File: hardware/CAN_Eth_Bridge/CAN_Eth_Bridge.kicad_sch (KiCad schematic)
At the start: 25 parts, among them J102 Global LV and CAN, J105 Conn_02x05_Odd_Even, J106 uart, SW101 SW_Push, U101 MCP2542FDxMF, U103 XMSM0G3507SDGS28R

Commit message: long 88 can stick
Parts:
- removed F101: ~1A, Fuse:Fuseholder_Blade_Mini_Keystone_3568, symbol Device:Fuse_Small
- removed J105: Conn_02x05_Odd_Even, Connector_PinHeader_1.27mm:PinHeader_2x05_P1.27mm_Vertical_SMD, symbol Connector_Generic:Conn_02x05_Odd_Even
- removed J106: uart, Connector_PinHeader_2.54mm:PinHeader_1x03_P2.54mm_Vertical, symbol Connector:Conn_01x03_Pin
- added C101, C102, C103: 220n, Capacitor_SMD:C_0805_2012Metric_Pad1.18x1.45mm_HandSolder, symbol Device:C_Small
- added D101: TS4148, Diode_SMD:D_0805_2012Metric_Pad1.15x1.40mm_HandSolder, symbol Device:D_Small
- added FL102: Choke_CommonMode_FerriteCore_1243, Inductor_SMD:L_CommonModeChoke_Coilcraft_1812CAN, symbol Filter:Choke_CommonMode_FerriteCore_1243
- added J101: Conn_01x05_Pin, Connector_PinHeader_2.54mm:PinHeader_1x05_P2.54mm_Vertical, symbol Connector:Conn_01x05_Pin
- added SW102: SW_DIP_x06, Button_Switch_SMD:SW_DIP_SPSTx06_Slide_Copal_CHS-06B_W7.62mm_P1.27mm, symbol Switch:SW_DIP_x06
- added U102: AP7384-50SA, Package_TO_SOT_SMD:SOT-23-3, symbol Regulator_Linear:AP7384-50SA
- added U104: AP7381-33SA-7, Package_TO_SOT_SMD:SOT-23, symbol Regulator_Linear:AP7381-33SA-7
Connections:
- net GLV- is gone; now on net GND: J102.2 (Pin_2)
- net +3.3V: now also U103.7 (VDD), C101.1, U104.2 (VO)
- net +5V: now also C102.1, U102.2 (VO)
- net GLV+: now also D101.2 (A)
- net GND: now also U103.8 (VSS), C101.2, C102.2, C103.2, J101.1 (Pin_1), U102.3 (GND), U104.3 (GND)
- net G_CAN+: now also FL102.1; no longer U101.7 (CANH)
- net G_CAN-: now also FL102.4; no longer U101.6 (CANL)
- net XDS_RXD: now also J101.3 (Pin_3)
- net XDS_TCK_SWDCLK: now also U103.23 (PA20/SWCLK), J101.5 (Pin_5)
- net XDS_TMS_SWDIO: now also U103.22 (PA19/SWDIO), J101.4 (Pin_4)
- net XDS_TXD: now also J101.2 (Pin_2)
- net vcore: now also U103.3 (VCORE)
- net at R112.1, SW101.1: now also U103.6 (NRST)
- net at U103.9 (PA2_/_ROSC): now also R111.2
- new net: C103.1, D101.1 (K), U102.1 (VI), U104.1 (VI)
- new net: FL102.3, U101.6 (CANL)
- new net: FL102.2, U101.7 (CANH)
- no-connect marks 4 -> 0
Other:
- removed sheet GLV PSU
- note added: "PSU"
- note removed: "- LV only. no HV present - (10,35]VDC GLV working - swap relays for >12VDC operation - IL assumed to share GLV GND - IL sense diode set for ~12VDC"
- note removed: "PWR"
- note removed: "SWD fish"
- moved on the sheet: C104, D103, D104, D105, D106, J102, R107, R108, R109, R110, U101, U103

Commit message: shuffled
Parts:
- renumbered C103 to C101, C104 to C102, C102 to C103, C101 to C104, C107 to C105, C108 to C106, C109 to C107, C110 to C108, D103 to D102, D105 to D103, D106 to D105, FL102 to FL101, J102 to J101, J101 to J102, R108 to R101, R110 to R102, R107 to R103, R109 to R104, R111 to R105, R112 to R106, SW102 to SW101, SW101 to SW102, U102 to U101, U104 to U102, U101 to U103, U103 to U104
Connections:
- net can.rx: now also U104.2 (PA27/RTC_OUT/A0_0)
- net can.tx: now also U104.1 (PA26/A0_1)
- net eth.MISO/POCI: now also U104.19 (PA16/A1_1/FCC_IN)
- net eth.MOSI/PICO: now also U104.21 (PA18/A1_3)
- net eth.SCLK: now also U104.20 (PA17/A1_2)

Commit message: hdd failure D:
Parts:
- removed C102: 220n, Capacitor_SMD:C_0805_2012Metric_Pad1.18x1.45mm_HandSolder, symbol Device:C_Small
- removed D103: red, LED_SMD:LED_0805_2012Metric_Pad1.15x1.40mm_HandSolder, symbol Device:LED_Small
- removed D104: yellow, LED_SMD:LED_0805_2012Metric_Pad1.15x1.40mm_HandSolder, symbol Device:LED_Small
- removed H101, H102, H103: MountingHole, MountingHole:MountingHole_3.2mm_M3, symbol Mechanical:MountingHole
- removed R101: 2.4k, Resistor_SMD:R_0805_2012Metric_Pad1.20x1.40mm_HandSolder, symbol Device:R_Small_US
- removed R106: 40.2k, Resistor_SMD:R_0805_2012Metric_Pad1.20x1.40mm_HandSolder, symbol Device:R_Small_US
- removed SW101: SW_DIP_x06, Button_Switch_SMD:SW_DIP_SPSTx06_Slide_Copal_CHS-06B_W7.62mm_P1.27mm, symbol Switch:SW_DIP_x06
- C107, C108: now not fitted; now left out of the parts list
- D102: value yellow -> green; mouser https://www.mouser.com/ProductDetail/Inolux/IN-S85CS5Y?qs=s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 -> https://www.mouser.com/ProductDetail/Inolux/IN-S85CS5G?qs=s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; specs 5mA, 75mW, 1.8Vf, 5Vr, 589nm, 35mcd -> 5mA, 90mW, 2.5Vf, 5Vr, 525nm, 230mcd; unit x1 0.22 -> 0.27; unit x10 0.15 -> 0.187
- R102: value 3.32k -> 2.4k; mouser https://www.mouser.com/ProductDetail/Walsin/WR08X3321FTL?qs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 -> https://www.mouser.com/ProductDetail/Panasonic/ERJ-P06J242V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; specs 3.32kOhm, 1%, 150V, 125mW, 100ppm, -55C, 155C -> (none); specs  (none) -> 500mW, 5%, 200ppm, 400V, -55C, +155C, anti-surge, TF; unit x1 0.10 -> 0.12; unit x10 0.019 -> 0.039
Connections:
- net led.BMSFault is gone; now on net +3.3V: R104.2
- net led.i2 is gone; now on net GND: R103.2
- net +3.3V: now also U104.24 (PA21/A1_7/VREF-)
- net GND: now also R102.2; no longer D102.1 (K), R102.1
- net XDS_RXD: now also J102.2 (Pin_2), U104.15 (PA10/CLK_OUT); no longer J102.3 (Pin_3)
- net XDS_TXD: now also J102.3 (Pin_3), U104.16 (PA11); no longer J102.2 (Pin_2)
- net eth.cs_N: now also U104.13 (PA6/HFCLK_IN/HFXOUT)
- net eth.irq_N: now also U104.12 (PA5/HFXIN/FCC_IN)
- net eth.reset_N: now also U104.14 (PA9_/_RTC_OUT_/_CLK_OUT)
- net led.i1: now also D102.2 (A), U104.28 (PA25/A0_2)
- net led.sched: now also U104.27 (PA24/A0_3)
- net at R103.1: now also D105.1 (K); no longer D102.2 (A)
- net at SW102.1, U104.6 (NRST): now also R104.1
- new net: D102.1 (K), R102.1
- no-connect marks 0 -> 8
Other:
- note removed: "BMS Fault"
- note removed: "indicator 2"
- moved on the sheet: D105, R103

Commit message: civilized note taking
and untaking !?!?!
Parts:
- added R101: 10, Resistor_SMD:R_0805_2012Metric_Pad1.20x1.40mm_HandSolder, symbol Device:R_Small_US
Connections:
- net GLV+: now also R101.2; no longer D101.2 (A)
- new net: D101.2 (A), R101.1
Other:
- note added: "dinky surge supression"
- moved on the sheet: C101, C103, C104, D101, U101, U102

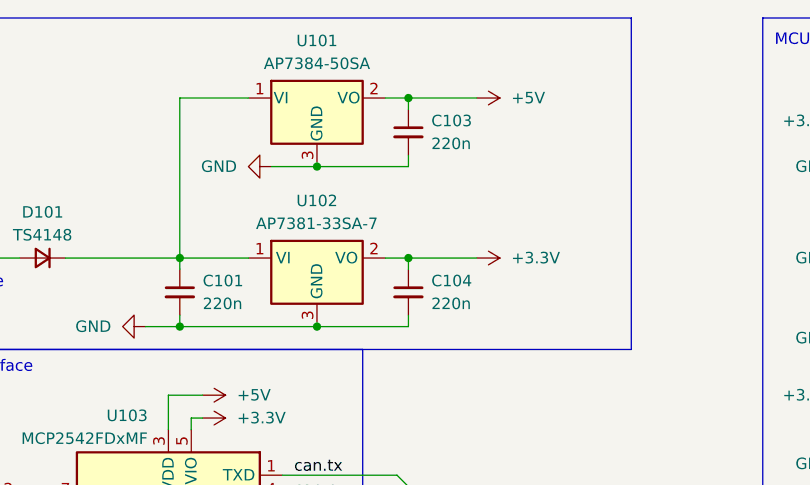
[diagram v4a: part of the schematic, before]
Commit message: pain :(
the 3v3 rail is a 1v rail. double deckering the LDO's didnt fix it :((( . needs new board
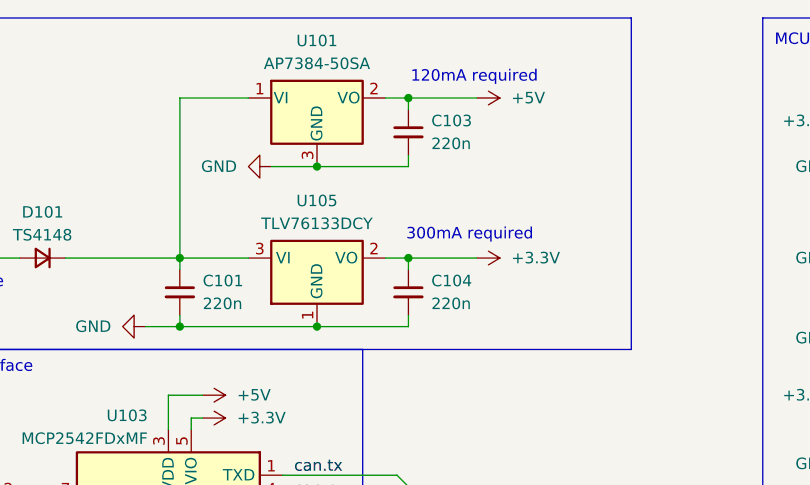
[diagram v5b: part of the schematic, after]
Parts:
- removed U102: AP7381-33SA-7, Package_TO_SOT_SMD:SOT-23, symbol Regulator_Linear:AP7381-33SA-7
- added U105: TLV76133DCY, Package_TO_SOT_SMD:SOT-223-3_TabPin2, symbol Regulator_Linear:TLV76133DCY
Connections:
- net +3.3V: now also U105.2 (VO)
- net GND: now also U105.1 (GND)
- net at C101.1, D101.1 (K), U101.1 (VI): now also U105.3 (VI)
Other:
- note added: "120mA required"
- note added: "300mA required"
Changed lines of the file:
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@@
 		)
 	)
+	(text "120mA required"
+		(exclude_from_sim no)
+		(at 114.554 20.066 0)
+		(effects
+			(font
+				(size 1.27 1.27)
+				(color 194 0 194 1)
+			)
+			(justify left bottom)
+		)
+	)
 	(text "indicator 1"
 		(exclude_from_sim no)
@@
 		)
 	)
+	(text "300mA required"
+		(exclude_from_sim no)
+		(at 114.046 37.592 0)
+		(effects
+			(font
+				(size 1.27 1.27)
+				(color 194 0 194 1)
+			)
+			(justify left bottom)
+		)
+	)
 	(text "dinky surge\nsupression"
 		(exclude_from_sim no)
@@
 	)
 	(junction
-		(at 104.14 46.99)
-		(diameter 0)
-		(color 0 0 0 0)
-	)
-	(junction
 		(at 88.9 46.99)
 		(diameter 0)
@@
 	)
 	(junction
+		(at 104.14 46.99)
+		(diameter 0)
+		(color 0 0 0 0)
+	)
+	(junction
 		(at 259.08 35.56)
 		(diameter 0)
@@
 	(wire
 		(pts
-			(xy 104.14 46.99) (xy 114.3 46.99)
+			(xy 88.9 46.99) (xy 104.14 46.99)
 		)
 		(stroke
@@
 	(wire
 		(pts
-			(xy 88.9 46.99) (xy 104.14 46.99)
-		)
-		(stroke
-			(width 0)
-			(type default)
-		)
-	)
-	(wire
-		(pts
 			(xy 114.3 21.59) (xy 111.76 21.59)
 		)
@@
 	(wire
 		(pts
+			(xy 104.14 46.99) (xy 114.3 46.99)
+		)
+		(stroke
+			(width 0)
+			(type default)
+		)
+	)
+	(wire
+		(pts
 			(xy 111.76 39.37) (xy 114.3 39.37)
 		)
@@
 	)
 	(symbol
+		(lib_id "Regulator_Linear:TLV76133DCY")
+		(at 104.14 39.37 0)
+		(unit 1)
+		(exclude_from_sim no)
+		(in_bom yes)
+		(on_board yes)
+		(dnp no)
+		(fields_autoplaced yes)
+		(property "Reference" "U105"
+			(at 104.14 33.02 0)
+			(effects
+				(font
+					(size 1.27 1.27)
+				)
+			)
+		)
+		(property "Value" "TLV76133DCY"
+			(at 104.14 35.56 0)
+			(effects
+				(font
+					(size 1.27 1.27)
+				)
+			)
+		)
+		(property "Footprint" "Package_TO_SOT_SMD:SOT-223-3_TabPin2"
+			(at 104.14 50.8 0)
+			(effects
+				(font
+					(size 1.27 1.27)
+				)
+				(hide yes)
+			)
+		)
+		(property "Datasheet" "https://www.ti.com/lit/ds/symlink/tlv761.pdf"
+			(at 104.14 53.34 0)
+			(effects
+				(font
+					(size 1.27 1.27)
+				)
+				(hide yes)
+			)
+		)
+		(property "Description" "3.3V, 1A, Low Noise, High-PSRR LDO Regulator, 2.5V...16V input, SOT-223"
+			(at 104.14 39.37 0)
+			(effects
+				(font
+					(size 1.27 1.27)
+				)
+				(hide yes)
+			)
+		)
+		(pin "2"
+		)
+		(pin "3"
+		)
+		(pin "1"
+		)
+		(instances
+			(project ""
+				(path "/20ac6af0-79b5-4ba6-aad3-75081d02c913"
+					(reference "U105")
+					(unit 1)
+				)
+			)
+		)
+	)
+	(symbol
 		(lib_id "zzLocalLibrary:XMSM0G3507SDGS28R")
 		(at 242.57 113.03 0)
@@
 					(unit 1)
 				)
-			)
-		)
-	)
-	(symbol
-		(lib_id "Regulator_Linear:AP7381-33SA-7")
-		(at 104.14 39.37 0)
-		(unit 1)
-		(exclude_from_sim no)
-		(in_bom yes)
-		(on_board yes)
-		(dnp no)
-		(fields_autoplaced yes)
-		(property "Reference" "U102"
-			(at 104.14 33.02 0)
-			(effects
-				(font
-					(size 1.27 1.27)
-				)
-			)
-		)
-		(property "Value" "AP7381-33SA-7"
-			(at 104.14 35.56 0)
-			(effects
-				(font
-					(size 1.27 1.27)
-				)
-			)
-		)
-		(property "Footprint" "Package_TO_SOT_SMD:SOT-23"
-			(at 104.14 49.53 0)
-			(effects
-				(font
-					(size 1.27 1.27)
-				)
-				(hide yes)
-			)
-		)
-		(property "Datasheet" "https://www.diodes.com/assets/Datasheets/AP7381.pdf"
-			(at 104.14 52.07 0)
-			(effects
-				(font
-					(size 1.27 1.27)
-				)
-				(hide yes)
-			)
-		)
-		(property "Description" "150mA Low Dropout Voltage Regulator, Fixed Output 3.3V, Wide Input Voltage Range 40V, SOT-23"
-			(at 104.14 54.61 0)
-			(effects
-				(font
-					(size 1.27 1.27)
-				)
-				(hide yes)
-			)
-		)
-		(property "mouser" "https://www.mouser.com/ProductDetail/Diodes-Incorporated/AP7381-33SA-7?qs=y6ZabgHbY%252ByfboEZm%252BnPlA%3D%3D"
-			(at 104.14 39.37 0)
-			(effects
-				(font
-					(size 1.27 1.27)
-				)
-				(hide yes)
-			)
-		)
-		(property "unit x10" "0.134"
-			(at 104.14 39.37 0)
-			(effects
-				(font
-					(size 1.27 1.27)
-				)
-				(hide yes)
-			)
-		)
-		(property "unit x1" "0.19"
-			(at 104.14 39.37 0)
-			(effects
-				(font
-					(size 1.27 1.27)
-				)
-				(hide yes)
-			)
-		)
-		(pin "1"
-		)
-		(pin "3"
-		)
-		(pin "2"
-		)
-		(instances
-			(project "CAN_Eth_Bridge"
-				(path "/20ac6af0-79b5-4ba6-aad3-75081d02c913"
-					(reference "U102")
-					(unit 1)
-				)

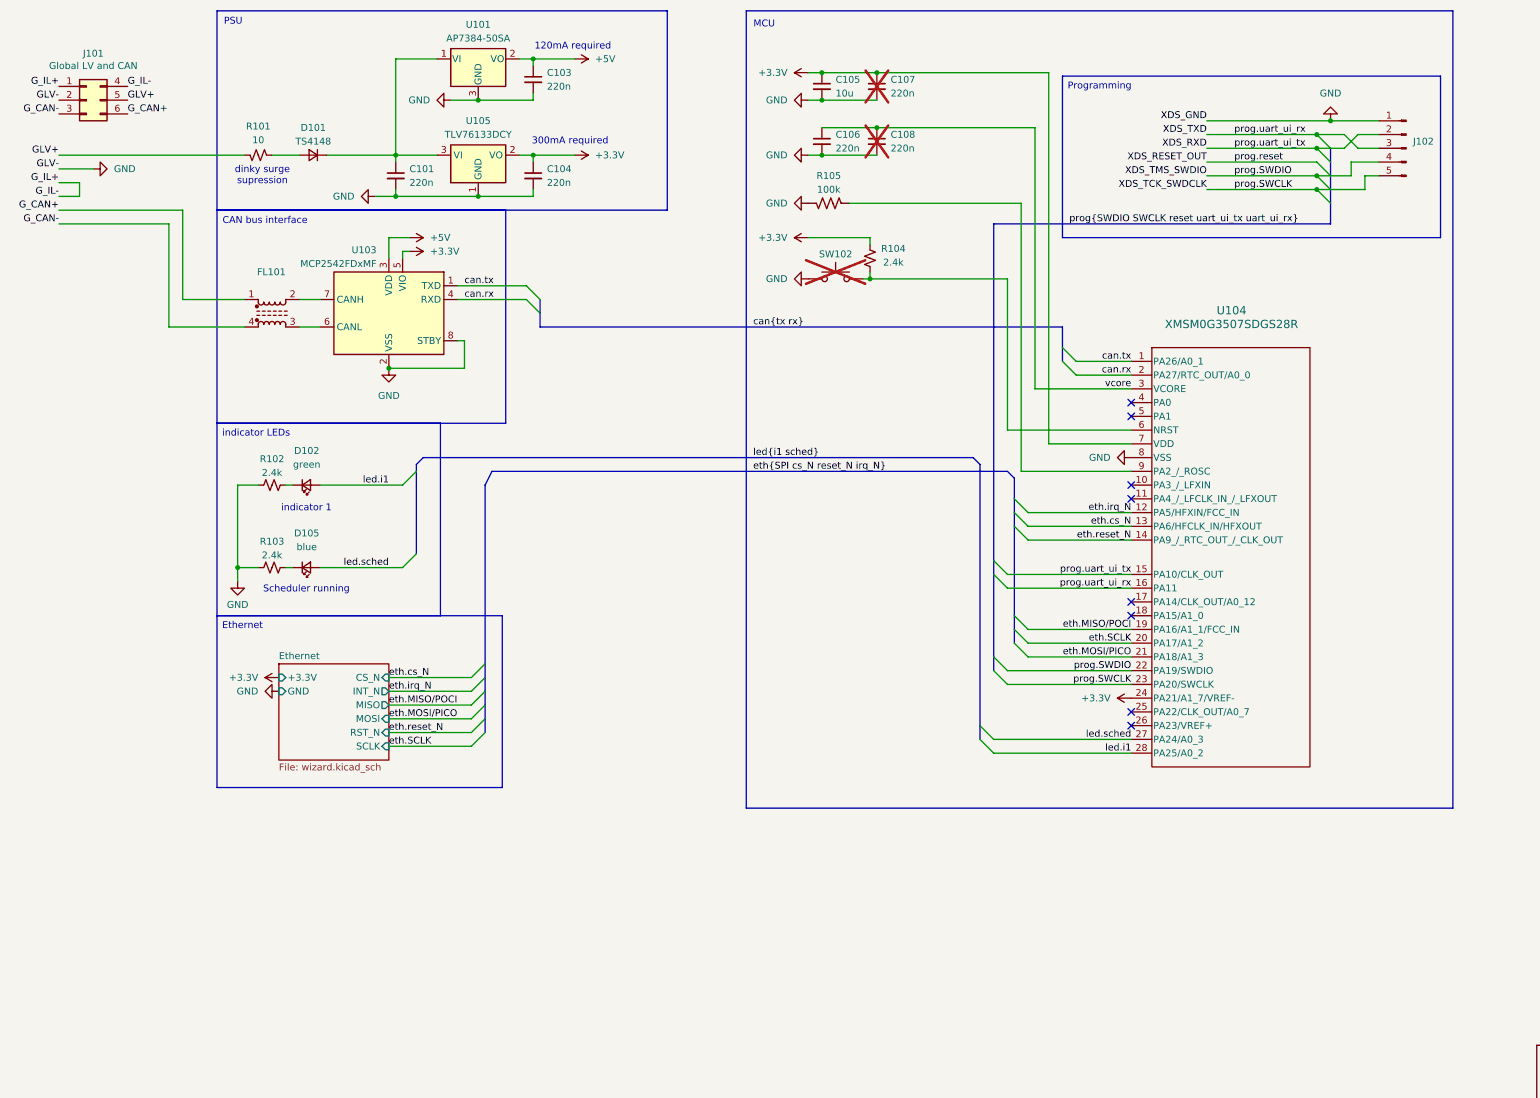
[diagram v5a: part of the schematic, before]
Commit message: super 3v3 rail
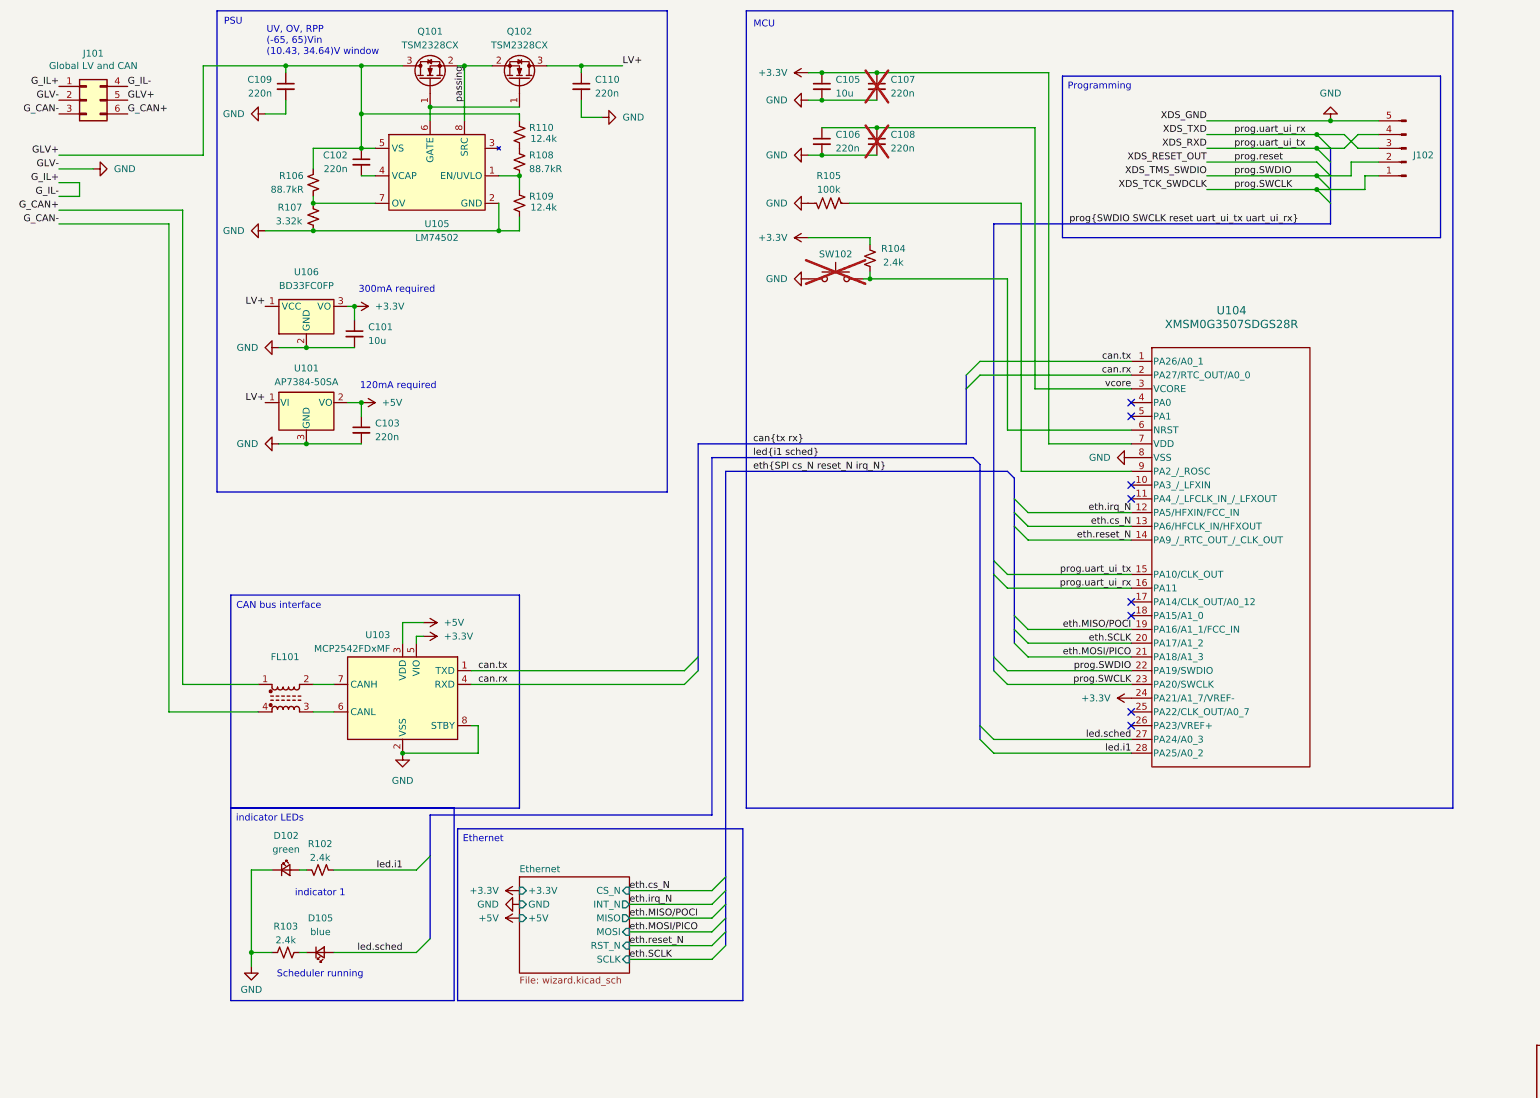
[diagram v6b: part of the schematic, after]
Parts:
- removed C104: 220n, Capacitor_SMD:C_0805_2012Metric_Pad1.18x1.45mm_HandSolder, symbol Device:C_Small
- removed D101: TS4148, Diode_SMD:D_0805_2012Metric_Pad1.15x1.40mm_HandSolder, symbol Device:D_Small
- removed R101: 10, Resistor_SMD:R_0805_2012Metric_Pad1.20x1.40mm_HandSolder, symbol Device:R_Small_US
- removed U105: TLV76133DCY, Package_TO_SOT_SMD:SOT-223-3_TabPin2, symbol Regulator_Linear:TLV76133DCY
- added C102, C109, C110: 220n, Capacitor_SMD:C_0805_2012Metric_Pad1.18x1.45mm_HandSolder, symbol Device:C_Small
- added Q101, Q102: TSM2328CX, Package_TO_SOT_SMD:SOT-23-3, symbol Transistor_FET:Q_NMOS_GSD
- added R106, R108: 88.7kR, Resistor_SMD:R_0805_2012Metric_Pad1.20x1.40mm_HandSolder, symbol Device:R_Small_US
- added R107: 3.32k, Resistor_SMD:R_0805_2012Metric_Pad1.20x1.40mm_HandSolder, symbol Device:R_Small_US
- added R109, R110: 12.4k, Resistor_SMD:R_0805_2012Metric_Pad1.20x1.40mm_HandSolder, symbol Device:R_Small_US
- added U105: LM74502, Package_TO_SOT_SMD:SOT-23-8_Handsoldering, symbol zzLocalLibrary:LM74502
- added U106: BD33FC0FP, Package_TO_SOT_SMD:TO-252-2, symbol Regulator_Linear:BD33FC0FP
- C101: value 220n -> 10u; footprint Capacitor_SMD:C_0805_2012Metric_Pad1.18x1.45mm_HandSolder -> Capacitor_SMD:C_1206_3216Metric_Pad1.33x1.80mm_HandSolder; mouser https://www.mouser.com/ProductDetail/Samsung-Electro-Mechanics/CL21B224KCFSFNE?qs=664zcAxDQ0l4Y1eUk6Zc1g%3D%3D -> https://www.mouser.com/ProductDetail/Samsung-Electro-Mechanics/CL31A106KBHNNNE?qs=sGAEpiMZZMsh%252B1woXyUXjxqcB7t9naYpzWmpMbMJIKQ%3D; specs 100VDC, X7R, 10%, -55C, +125C, 220nF -> 10uF, 50VDC, X5R, 10%, -55C, +85C; unit x1 0.054 -> (none); unit x10 0.054 -> 0.07
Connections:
- net +3.3V: now also C101.1, U106.3 (VO)
- net GLV+: now also C102.1, C109.1, Q101.3 (D), R106.2, R110.2, U105.5 (VS)
- net GND: now also D102.1 (K), J102.5 (Pin_5), C109.2, C110.2, R107.1, R109.1, U105.2 (GND), U106.2 (GND); no longer J102.1 (Pin_1), R102.2
- net XDS_RXD: now also J102.4 (Pin_4); no longer J102.2 (Pin_2)
- net XDS_TCK_SWDCLK: now also J102.1 (Pin_1); no longer J102.5 (Pin_5)
- net XDS_TMS_SWDIO: now also J102.2 (Pin_2); no longer J102.4 (Pin_4)
- net led.i1: now also R102.2; no longer D102.2 (A)
- net LV+: now reaches U101.1 (VI)
- net LV+: now also C110.1, Q102.3 (D), U106.1 (VCC); no longer C101.1
- net at R102.1: now also D102.2 (A); no longer D102.1 (K)
- new net: Q101.1 (G), Q102.1 (G), U105.6 (GATE)
- new net: R108.1, R109.2, U105.1 (EN/UVLO)
- new net: R106.1, R107.2, U105.7 (OV)
- new net: C102.2, U105.4 (VCAP)
- new net: R108.2, R110.1
- new net passing: Q101.2 (S), Q102.2 (S), U105.8 (SRC)
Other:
- sheet Ethernet ports: added +5V; removed none
- note added: "UV, OV, RPP (-65, 65)Vin (10.43, 34.64)V window"
- note removed: "dinky surge supression"
- moved on the sheet: C103, D102, D105, FL101, J102, R102, R103, U101, U103

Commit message: bridge v2
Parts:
- C109: now not fitted; now left out of the parts list
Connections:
- net GND: now also J102.1 (Pin_1); no longer J102.5 (Pin_5)
- net XDS_RXD: now also J102.2 (Pin_2); no longer J102.4 (Pin_4)
- net XDS_TCK_SWDCLK: now also J102.5 (Pin_5); no longer J102.1 (Pin_1)
- net XDS_TMS_SWDIO: now also J102.4 (Pin_4); no longer J102.2 (Pin_2)
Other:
- moved on the sheet: J102
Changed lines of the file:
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@@
 	(symbol
 		(lib_id "Connector:Conn_01x05_Pin")
-		(at 275.59 38.1 180)
+		(at 275.59 38.1 0)
+		(mirror y)
 		(unit 1)
 		(exclude_from_sim no)
@@
 		(dnp no)
 		(property "Reference" "J102"
-			(at 276.86 39.3701 0)
+			(at 276.86 36.8299 0)
 			(effects
 				(font
@@
 		)
 		(property "Value" "Conn_01x05_Pin"
-			(at 276.86 36.8301 0)
+			(at 276.86 39.3699 0)
 			(effects
 				(font
@@
 		(unit 1)
 		(exclude_from_sim no)
-		(in_bom yes)
-		(on_board yes)
-		(dnp no)
+		(in_bom no)
+		(on_board no)
+		(dnp yes)
 		(property "Reference" "C109"
 			(at 66.04 25.4062 0)
